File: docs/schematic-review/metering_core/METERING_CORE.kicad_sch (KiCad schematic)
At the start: 56 parts, among them U2 ATM90E26-YU, U4 ISO6721BD, U5 MAX3487E

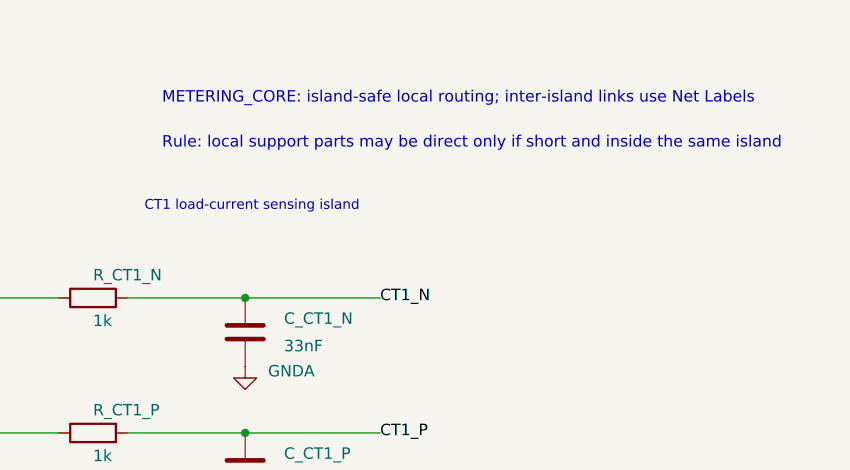
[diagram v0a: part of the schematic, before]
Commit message: Address Gemini schematic junction feedback
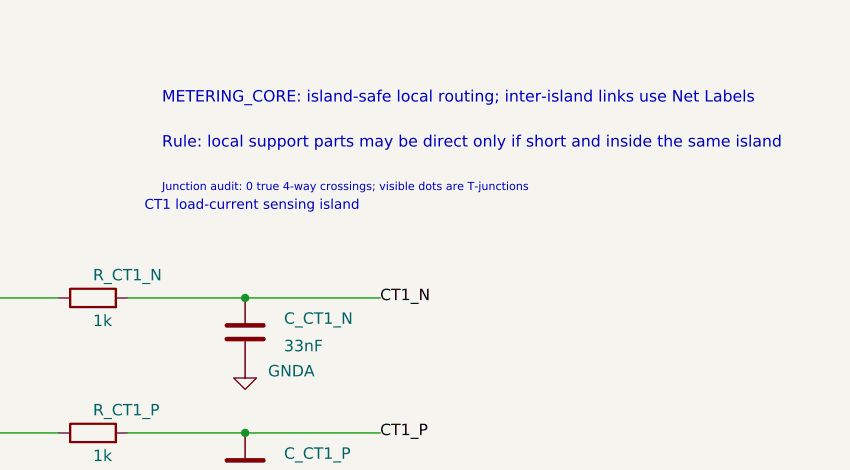
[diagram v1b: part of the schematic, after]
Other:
- note added: "Junction audit: 0 true 4-way crossings; visible dots are T-junctions"
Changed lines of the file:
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@@
+		)
+	)
+	(text "Junction audit: 0 true 4-way crossings; visible dots are T-junctions"
+		(exclude_from_sim no)
+		(at 65.692 29.75 0)
+		(effects
+			(font
+				(size 0.9 0.9)
+			)
+			(justify left)
 		)
 	)

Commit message: Fix metering schematic visual review artifacts
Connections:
- net DGND: no longer U_MCU.18 (VSS), U_MCU.31 (VSS), U_MCU.63 (VSS)
- net GNDA: now also U_MCU.63 (VSS); no longer U_MCU.12 (VSSA)
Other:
- note added: "MCU_PLC SPI header"
- note removed: "MCU_PLC SPI pin header - separate from MCU_DCU UART and MCU_METER SPI"
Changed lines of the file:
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@@
 	(text "MCU Reset Island - MCU_RESET pull-up and RC filter"
 		(exclude_from_sim no)
-		(at 220 247 0)
+		(at 220 241 0)
 		(effects
 			(font
-				(size 1.27 1.27)
+				(size 0.9 0.9)
 			)
 			(justify left bottom)
@@
 	)
 	(label "DC12V_IN"
-		(at 20.32 267.97 180)
+		(at 25.4 267.97 180)
 		(effects
 			(font
-				(size 1.27 1.27)
+				(size 0.9 0.9)
 			)
 			(justify right)
@@
 	)
 	(label "DC12V_GND"
-		(at 20.32 273.05 180)
+		(at 25.4 273.05 180)
 		(effects
 			(font
-				(size 1.27 1.27)
+				(size 0.9 0.9)
 			)
 			(justify right)
@@
 		(dnp no)
 		(property "Reference" "U_MCU"
-			(at 314.76 196.99 0)
+			(at 314.76 203.2 0)
 			(show_name no)
 			(do_not_autoplace no)
@@
 		)
 		(property "Value" "STM32L053R8T6"
-			(at 340.16 196.99 0)
+			(at 340.16 203.2 0)
 			(show_name no)
 			(do_not_autoplace no)
@@
 		)
 	)
-	(text "MCU_PLC SPI pin header - separate from MCU_DCU UART and MCU_METER SPI"
+	(text "MCU_PLC SPI header"
 		(exclude_from_sim no)
-		(at 344 12 0)
+		(at 336 35 0)
 		(effects
 			(font
-				(size 1.1 1.1)
+				(size 0.9 0.9)
 				(bold yes)
 			)

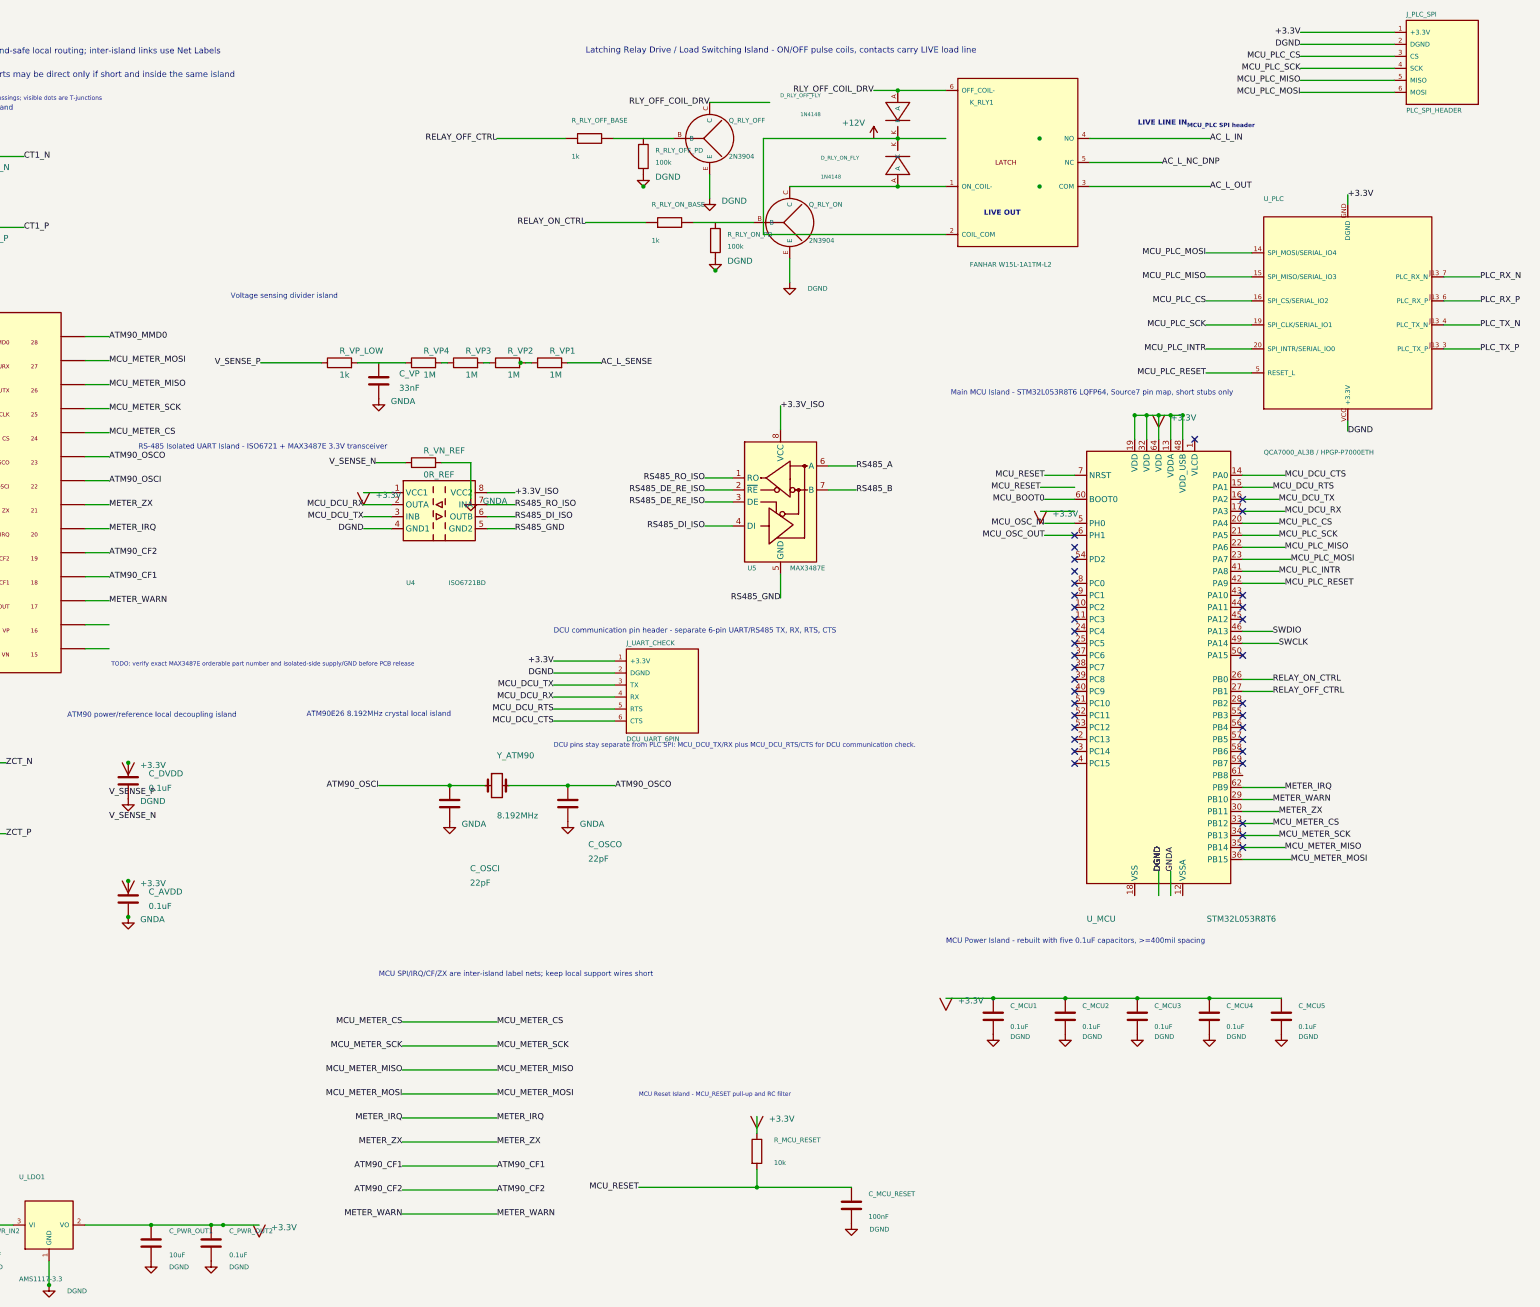
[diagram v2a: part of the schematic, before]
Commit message: Fix metering schematic visual clearance hotspots
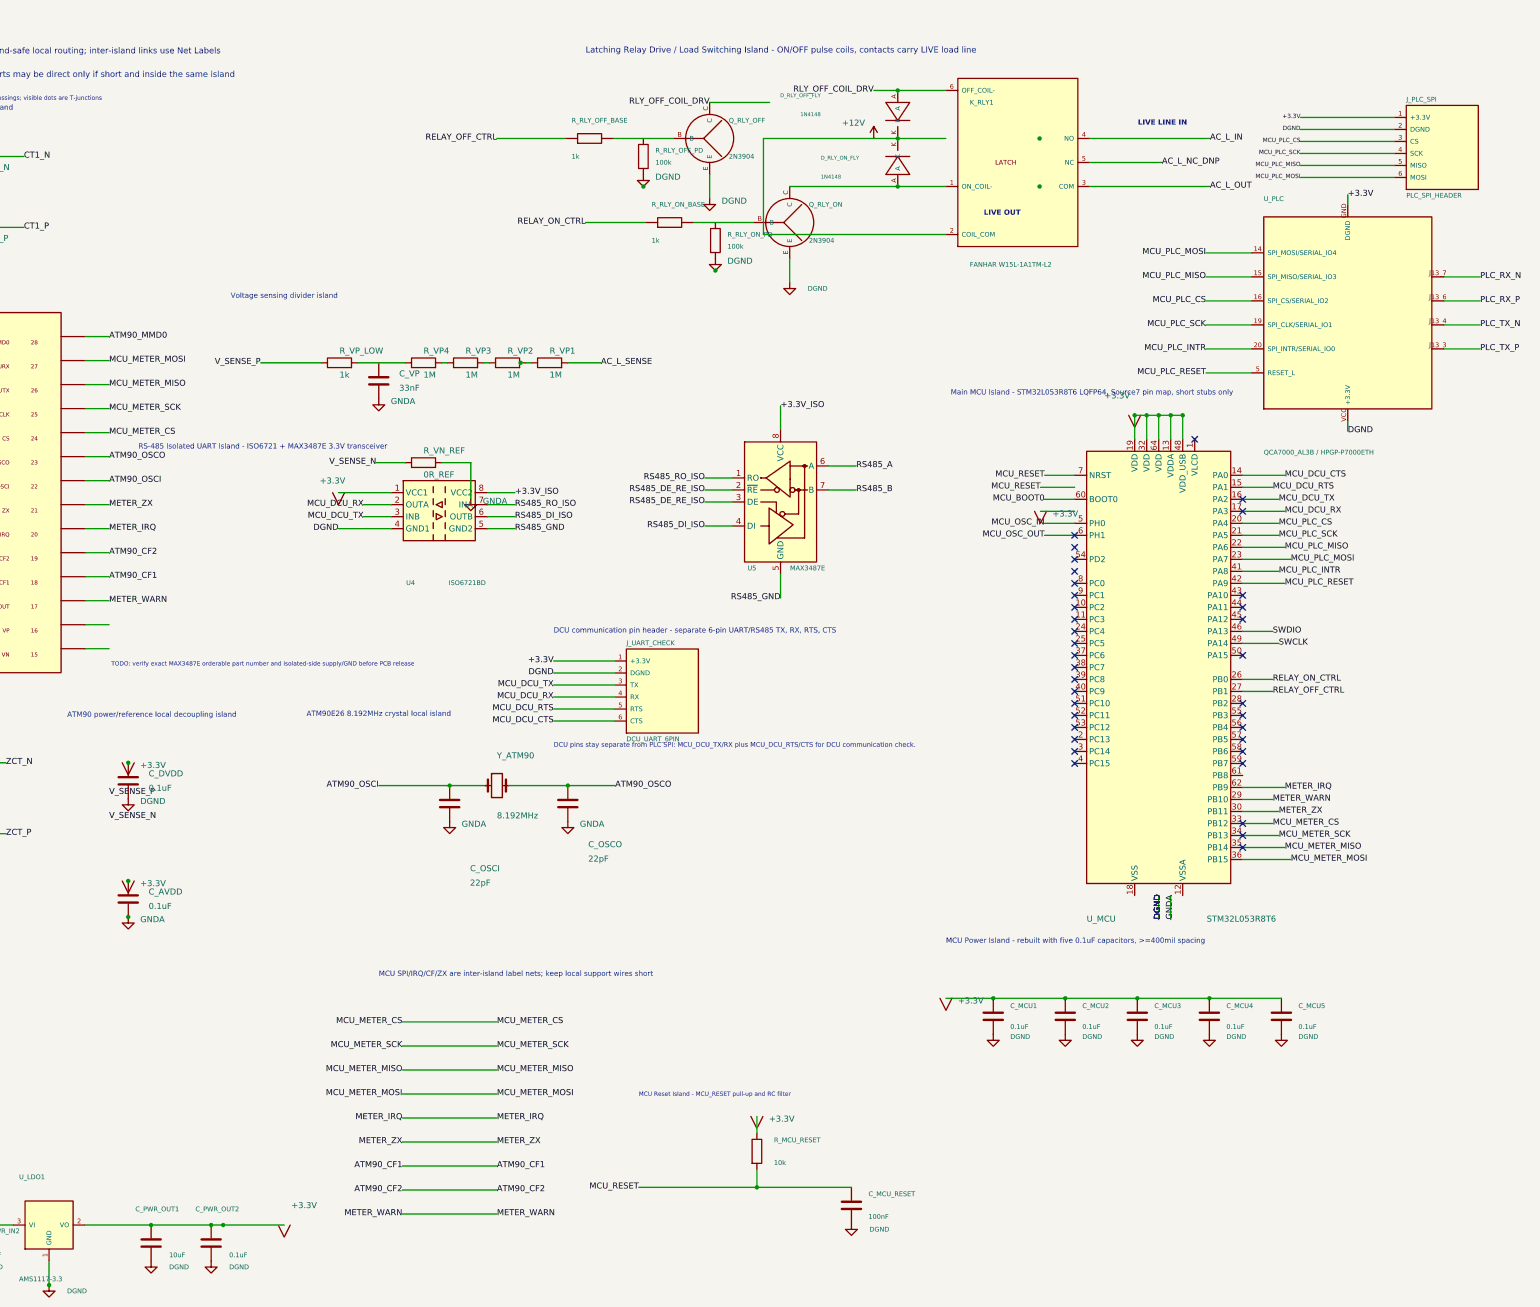
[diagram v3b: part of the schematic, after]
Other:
- note added: "PLC SPI"
- note removed: "MCU_PLC SPI header"
- moved on the sheet: J_PLC_SPI
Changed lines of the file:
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@@
 	(wire
 		(pts
-			(xy 330 198.26) (xy 330 193.18)
+			(xy 330 198.26) (xy 330 203.34)
 		)
 		(stroke
@@
 	(wire
 		(pts
-			(xy 167.64 113.03) (xy 161.8 113.03)
+			(xy 167.64 113.03) (xy 156.5 113.03)
 		)
 		(stroke
@@
 	(wire
 		(pts
-			(xy 167.64 120.65) (xy 161.8 120.65)
+			(xy 167.64 120.65) (xy 156.5 120.65)
 		)
 		(stroke
@@
 	(wire
 		(pts
-			(xy 332.54 198.26) (xy 332.54 193.18)
+			(xy 332.54 198.26) (xy 332.54 203.34)
 		)
 		(stroke
@@
 	(wire
 		(pts
-			(xy 102.87 267.97) (xy 139.7 267.97)
+			(xy 102.87 267.97) (xy 145 267.97)
 		)
 		(stroke
@@
 	)
 	(label "DGND"
-		(at 330 193.18 90)
+		(at 330 203.34 90)
 		(effects
 			(font
@@
 	)
 	(label "DGND"
-		(at 161.8 120.65 180)
+		(at 156.5 120.65 180)
 		(effects
 			(font
@@
 	)
 	(label "DGND"
-		(at 330 193.18 90)
+		(at 330 203.34 90)
 		(effects
 			(font
@@
 	)
 	(label "DGND"
-		(at 330 193.18 90)
+		(at 330 203.34 90)
 		(effects
 			(font
@@
 	(symbol
 		(lib_id "power:+3.3V")
-		(at 330 96.66 0)
+		(at 324.92 96.66 0)
 		(unit 1)
 		(body_style 1)
@@
 		(dnp no)
 		(property "Reference" "#PWR_AUTO_33V_003"
-			(at 332.54 92.85 0)
+			(at 327.46 92.85 0)
 			(hide yes)
 			(show_name no)
@@
 		)
 		(property "Value" "+3.3V"
-			(at 332.54 97.168 0)
+			(at 318.5 92.5 0)
 			(show_name no)
 			(do_not_autoplace no)
@@
 		)
 		(property "Footprint" ""
-			(at 330 96.66 0)
+			(at 324.92 96.66 0)
 			(show_name no)
 			(do_not_autoplace no)
@@
 		)
 		(property "Datasheet" ""
-			(at 330 96.66 0)
+			(at 324.92 96.66 0)
 			(show_name no)
 			(do_not_autoplace no)
@@
 		)
 		(property "Description" ""
-			(at 330 96.66 0)
+			(at 324.92 96.66 0)
 			(show_name no)
 			(do_not_autoplace no)
@@
 	(symbol
 		(lib_id "power:+3.3V")
-		(at 161.8 113.03 0)
+		(at 156.5 113.03 0)
 		(unit 1)
 		(body_style 1)
@@
 		(dnp no)
 		(property "Reference" "#PWR_AUTO_33V_006"
-			(at 164.34 109.22 0)
+			(at 159.04 109.22 0)
 			(hide yes)
 			(show_name no)
@@
 		)
 		(property "Value" "+3.3V"
-			(at 164.34 113.538 0)
+			(at 152.5 110.5 0)
 			(show_name no)
 			(do_not_autoplace no)
@@
 		)
 		(property "Footprint" ""
-			(at 161.8 113.03 0)
+			(at 156.5 113.03 0)
 			(show_name no)
 			(do_not_autoplace no)
@@
 		)
 		(property "Datasheet" ""
-			(at 161.8 113.03 0)
+			(at 156.5 113.03 0)
 			(show_name no)
 			(do_not_autoplace no)
@@
 		)
 		(property "Description" ""
-			(at 161.8 113.03 0)
+			(at 156.5 113.03 0)
 			(show_name no)
 			(do_not_autoplace no)
@@
 	)
 	(label "GNDA"
-		(at 332.54 193.18 90)
+		(at 332.54 203.34 90)
 		(effects
 			(font
@@
 	)
 	(label "DGND"
-		(at 330 193.18 90)
+		(at 330 203.34 90)
 		(effects
 			(font
@@
 	(symbol
 		(lib_id "power:+3.3V")
-		(at 139.7 267.97 0)
+		(at 145 267.97 0)
 		(unit 1)
 		(body_style 1)
@@
 		(dnp no)
 		(property "Reference" "#PWR_AUTO_33V_010"
-			(at 142.24 264.16 0)
+			(at 147.54 264.16 0)
 			(hide yes)
 			(show_name no)
@@
 		)
 		(property "Value" "+3.3V"
-			(at 142.24 268.478 0)
+			(at 146.5 263.8 0)
 			(show_name no)
 			(do_not_autoplace no)
@@
 		)
 		(property "Footprint" ""
-			(at 139.7 267.97 0)
+			(at 145 267.97 0)
 			(show_name no)
 			(do_not_autoplace no)
@@
 		)
 		(property "Datasheet" ""
-			(at 139.7 267.97 0)
+			(at 145 267.97 0)
 			(show_name no)
 			(do_not_autoplace no)
@@
 		)
 		(property "Description" ""
-			(at 139.7 267.97 0)
+			(at 145 267.97 0)
 			(show_name no)
 			(do_not_autoplace no)
@@
 		(dnp no)
 		(property "Reference" "C_PWR_OUT1"
-			(at 120.65 269.24 0)
+			(at 113.5 264.6 0)
 			(show_name no)
 			(do_not_autoplace no)
@@
 		(dnp no)
 		(property "Reference" "C_PWR_OUT2"
-			(at 133.35 269.24 0)
+			(at 126.2 264.6 0)
 			(show_name no)
 			(do_not_autoplace no)
@@
 		)
 	)
-	(text "MCU_PLC SPI header"
+	(text "PLC SPI"
 		(exclude_from_sim no)
-		(at 336 35 0)
+		(at 372 51 0)
 		(effects
 			(font
-				(size 0.9 0.9)
+				(size 0.01 0.01)
 				(bold yes)
 			)
@@
 	(symbol
 		(lib_id "SmartLoad:PLC_SPI_6PIN_HEADER")
-		(at 390.00 22.00 0)
+		(at 390.00 40.00 0)
 		(unit 1)
 		(body_style 1)
@@
 		(in_pos_files yes)
 		(dnp no)
-		(property "Reference" "J_PLC_SPI" (at 382.38 11.84 0) (show_name no) (do_not_autoplace no) (effects (font (size 1 1)) (justify left)))
-		(property "Value" "PLC_SPI_HEADER" (at 382.38 32.16 0) (show_name no) (do_not_autoplace no) (effects (font (size 1 1)) (justify left)))
-		(property "Footprint" "Connector_PinHeader_2.54mm:PinHeader_1x06_P2.54mm_Vertical" (at 390.00 22.00 0) (hide yes) (show_name no) (do_not_autoplace no) (effects (font (size 1 1))))
-		(property "Datasheet" "" (at 390.00 22.00 0) (hide yes) (show_name no) (do_not_autoplace no) (effects (font (size 1 1))))
-		(property "Description" "MCU-to-PLC SPI header only: MCU_PLC_CS/SCK/MISO/MOSI are separate PA4-PA7 nets; no DCU UART or METER SPI nets here" (at 390.00 22.00 0) (hide yes) (show_name no) (do_not_autoplace no) (effects (font (size 1 1))))
+		(property "Reference" "J_PLC_SPI" (at 382.38 29.84 0) (show_name no) (do_not_autoplace no) (effects (font (size 1 1)) (justify left)))
+		(property "Value" "PLC_SPI_HEADER" (at 382.38 50.16 0) (show_name no) (do_not_autoplace no) (effects (font (size 1 1)) (justify left)))
+		(property "Footprint" "Connector_PinHeader_2.54mm:PinHeader_1x06_P2.54mm_Vertical" (at 390.00 40.00 0) (hide yes) (show_name no) (do_not_autoplace no) (effects (font (size 1 1))))
+		(property "Datasheet" "" (at 390.00 40.00 0) (hide yes) (show_name no) (do_not_autoplace no) (effects (font (size 1 1))))
+		(property "Description" "MCU-to-PLC SPI header only: MCU_PLC_CS/SCK/MISO/MOSI are separate PA4-PA7 nets; no DCU UART or METER SPI nets here" (at 390.00 40.00 0) (hide yes) (show_name no) (do_not_autoplace no) (effects (font (size 1 1))))
 		(pin "1")
 		(pin "2")
@@
 	(wire
 		(pts
-			(xy 360 15.65) (xy 379.84 15.65)
+			(xy 360 33.65) (xy 379.84 33.65)
 		)
 		(stroke
@@
 	)
 	(label "+3.3V"
-		(at 360 15.65 180)
+		(at 360 33.65 180)
 		(effects
 			(font
-				(size 1.27 1.27)
+				(size 0.9 0.9)
 			)
 			(justify right)
@@
 	(wire
 		(pts
-			(xy 360 18.19) (xy 379.84 18.19)
+			(xy 360 36.19) (xy 379.84 36.19)
 		)
 		(stroke
@@
 	)
 	(label "DGND"
-		(at 360 18.19 180)
+		(at 360 36.19 180)
 		(effects
 			(font
-				(size 1.27 1.27)
+				(size 0.9 0.9)
 			)
 			(justify right)
@@
 	(wire
 		(pts
-			(xy 360 20.73) (xy 379.84 20.73)
+			(xy 360 38.73) (xy 379.84 38.73)
 		)
 		(stroke
@@
 	)
 	(label "MCU_PLC_CS"
-		(at 360 20.73 180)
+		(at 360 38.73 180)
 		(effects
 			(font
-				(size 1.27 1.27)
+				(size 0.9 0.9)
 			)
 			(justify right)
@@
 	(wire
 		(pts
-			(xy 360 23.27) (xy 379.84 23.27)
+			(xy 360 41.27) (xy 379.84 41.27)
 		)
 		(stroke
@@
 	)
 	(label "MCU_PLC_SCK"
-		(at 360 23.27 180)
+		(at 360 41.27 180)
 		(effects
 			(font
-				(size 1.27 1.27)
+				(size 0.9 0.9)
 			)
 			(justify right)
@@
 	(wire
 		(pts
-			(xy 360 25.81) (xy 379.84 25.81)
+			(xy 360 43.81) (xy 379.84 43.81)
 		)
 		(stroke
@@
 	)
 	(label "MCU_PLC_MISO"
-		(at 360 25.81 180)
+		(at 360 43.81 180)
 		(effects
 			(font
-				(size 1.27 1.27)
+				(size 0.9 0.9)
 			)
 			(justify right)
@@
 	(wire
 		(pts
-			(xy 360 28.35) (xy 379.84 28.35)
+			(xy 360 46.35) (xy 379.84 46.35)
 		)
 		(stroke
@@
 	)
 	(label "MCU_PLC_MOSI"
-		(at 360 28.35 180)
+		(at 360 46.35 180)
 		(effects
 			(font
-				(size 1.27 1.27)
+				(size 0.9 0.9)
 			)
 			(justify right)
